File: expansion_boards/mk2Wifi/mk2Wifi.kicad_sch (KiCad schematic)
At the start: 21 parts, among them J2 USB_C_Receptacle_USB2.0, J4 OLED, SW1 SW_Push, U1 ESP32-C3-MINI-1, U2 AP2112K-3.3

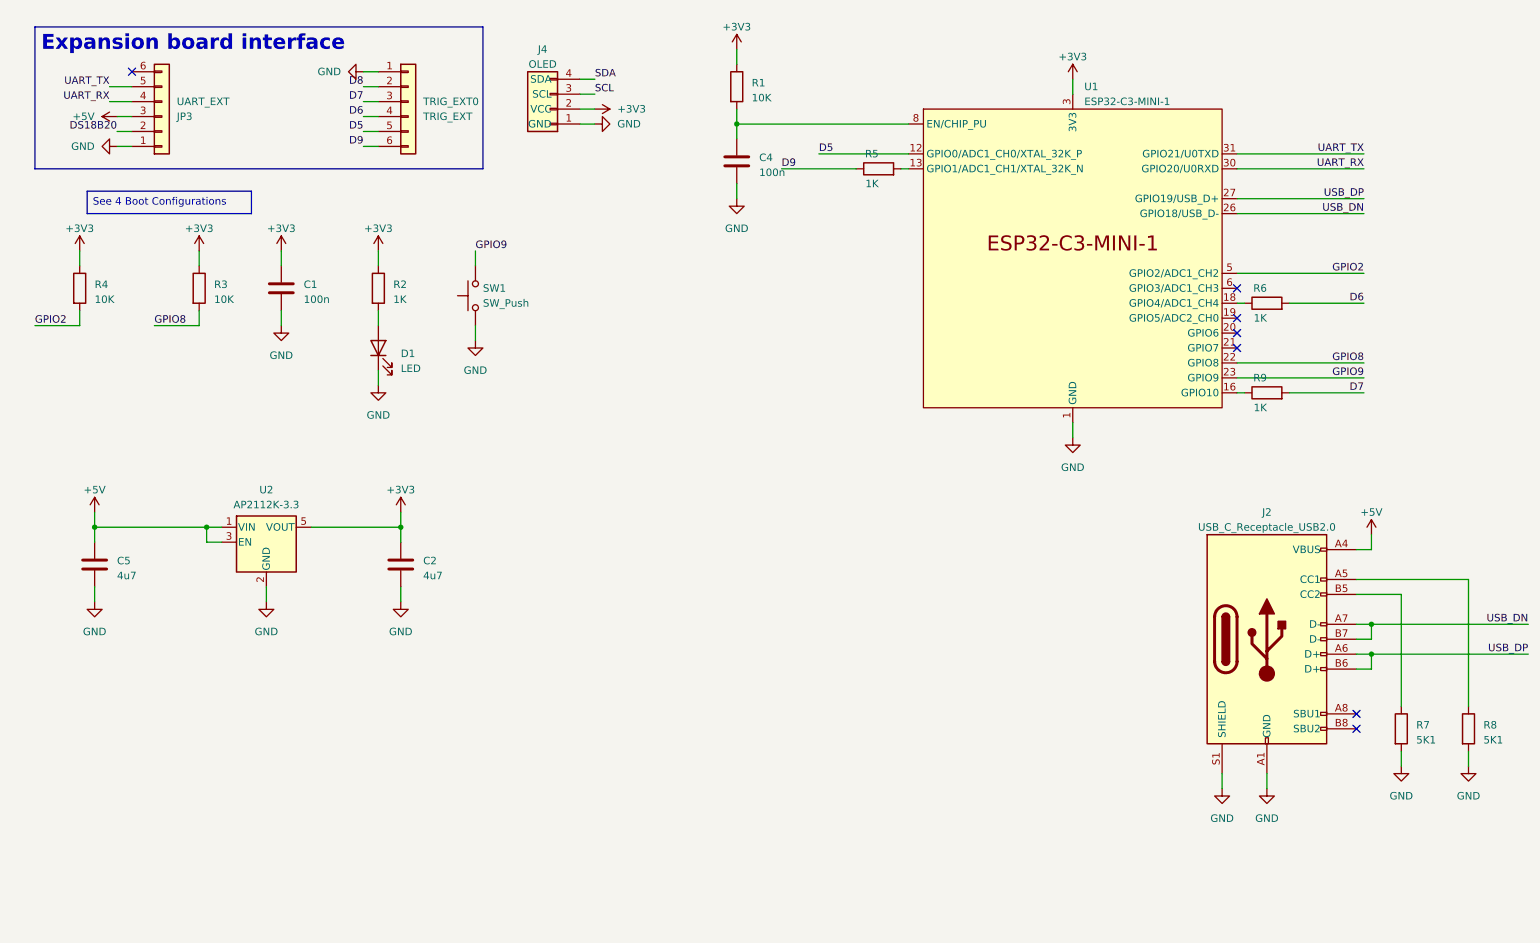
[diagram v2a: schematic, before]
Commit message: Wire remaining ESP32-C3 GPIOs and fix mk2Wifi ERC errors
Connect GPIO3 (DS18B20), GPIO5 (SDA), GPIO6 (SCL) directly and
GPIO7 (D8) through R11 (1K) protection resistor. Fix duplicate
power symbol references (#PWR01/03/04/08), add UserDef symbol
library to sym-lib-table, and add PWR_FLAG symbols to +5V, +3.3V,
and GND nets to resolve all ERC errors.

Co-Authored-By: Claude Opus 4.6 <noreply@anthropic.com>
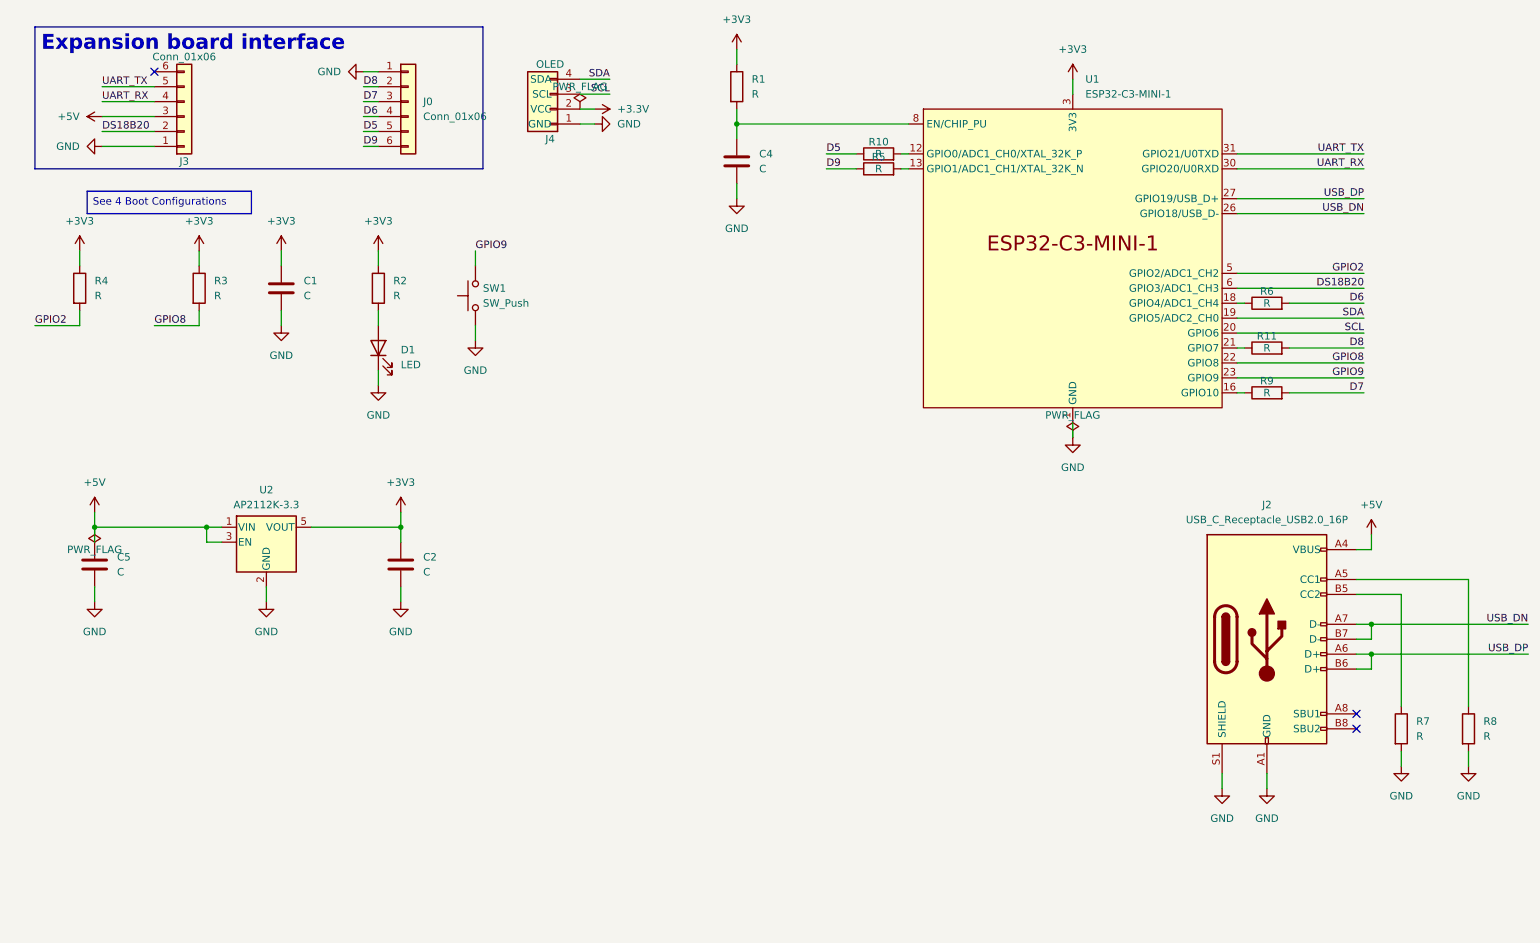
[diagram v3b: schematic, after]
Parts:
- added R10, R11: R, symbol Device:R
- C1, C4: value 100n -> C; footprint Capacitor_SMD:C_0402_1005Metric -> (none); LCSC PN C1525 -> (none)
- C2, C5: value 4u7 -> C; footprint Capacitor_SMD:C_0603_1608Metric -> (none); LCSC PN C19666 -> (none)
- D1: footprint LED_SMD:LED_0603_1608Metric -> (none); LCSC PN C2286 -> (none)
- J0: renamed from TRIG_EXT0; value TRIG_EXT -> Conn_01x06; footprint Connector_PinSocket_2.54mm:PinSocket_1x06_P2.54mm_Vertical -> (none)
- J2: value USB_C_Receptacle_USB2.0 -> USB_C_Receptacle_USB2.0_16P; footprint valcon-usb:CSP-USC16-TR -> (none); symbol Connector:USB_C_Receptacle_USB2.0 -> Connector:USB_C_Receptacle_USB2.0_16P; LCSC PN C2765186 -> (none)
- J3: renamed from JP3; value UART_EXT -> Conn_01x06; footprint Connector_PinSocket_2.54mm:PinSocket_1x06_P2.54mm_Vertical -> (none)
- J4: footprint Connector_Molex:Molex_SL_171971-0004_1x04_P2.54mm_Vertical -> (none); Option X -> (none)
- R1, R3, R4: value 10K -> R; footprint Resistor_SMD:R_0402_1005Metric -> (none); LCSC PN C25744 -> (none)
- R2: value 1K -> R; footprint Resistor_SMD:R_0402_1005Metric -> (none); LCSC PN C11702 -> (none)
- R5, R6, R9: value 1K -> R; footprint Resistor_SMD:R_0402_1005Metric -> (none)
- R7, R8: value 5K1 -> R; footprint Resistor_SMD:R_0402_1005Metric -> (none); LCSC PN C25905 -> (none)
- SW1: footprint Button_Switch_SMD:SW_Tactile_SPST_NO_Straight_CK_PTS636Sx25SMTRLFS -> (none); LCSC PN C2689642 -> (none)
- U1: LCSC PN C2838502 -> (none)
- U2: LCSC PN C23380830 -> (none)
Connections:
- net +3V3: no longer J4.2 (VCC)
- net D5: now also R10.1; no longer U1.12 (GPIO0/ADC1_CH0/XTAL_32K_P)
- net D8: now also R11.2
- net DS18B20: now also U1.6 (GPIO3/ADC1_CH3)
- net SCL: now also U1.20 (GPIO6)
- net SDA: now also U1.19 (GPIO5/ADC2_CH0)
- net at U1.21 (GPIO7): now also R11.1
- new net: R10.2, U1.12 (GPIO0/ADC1_CH0/XTAL_32K_P)
- new net +3.3V: J4.2 (VCC)
- no-connect marks 7 -> 3
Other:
- moved on the sheet: J3

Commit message: Assign footprints and values to all mk2Wifi components
Set resistor values (1K, 5K1, 10K) and 0402 footprints for R1-R11,
capacitor values (100n, 4u7) with 0402/0603 footprints for C1-C5,
and footprints for D1 (LED 0603), SW1 (CK PTS636S tactile), J0 and
J3 (PinSocket 1x06). Values and footprints match emonWiFi reference
design by circuit function.

Co-Authored-By: Claude Opus 4.6 <noreply@anthropic.com>
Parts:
- C1, C4: value C -> 100n; footprint (none) -> Capacitor_SMD:C_0402_1005Metric
- C2, C5: value C -> 4u7; footprint (none) -> Capacitor_SMD:C_0603_1608Metric
- D1: footprint (none) -> LED_SMD:LED_0603_1608Metric
- J0, J3: footprint (none) -> Connector_PinSocket_2.54mm:PinSocket_1x06_P2.54mm_Vertical
- J2: footprint (none) -> valcon-usb:CSP-USC16-TR
- J4: footprint (none) -> Connector_Molex:Molex_SL_171971-0004_1x04_P2.54mm_Vertical
- R1, R3, R4: value R -> 10K; footprint (none) -> Resistor_SMD:R_0402_1005Metric
- R10, R11, R2, R5, R6, R9: value R -> 1K; footprint (none) -> Resistor_SMD:R_0402_1005Metric
- R7, R8: value R -> 5K1; footprint (none) -> Resistor_SMD:R_0402_1005Metric
- SW1: footprint (none) -> Button_Switch_SMD:SW_Tactile_SPST_NO_Straight_CK_PTS636Sx25SMTRLFS

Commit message: Finalize mk2Wifi PCB layout, project settings, and 3D model
Update PCB layout with component placement and routing for all
newly footprinted parts. Adjust zone clearance (0.25mm) and via
sizes (0.8/0.4mm) in project settings. Add UserDef footprint
library to fp-lib-table. Include ESP32-C3-MINI-1 STEP 3D model.

Co-Authored-By: Claude Opus 4.6 <noreply@anthropic.com>
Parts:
- J0: value Conn_01x06 -> TRIG_EXT
- J3: value Conn_01x06 -> UART_EXT
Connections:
- net at R9.1: now also U1.13 (GPIO1/ADC1_CH1/XTAL_32K_N); no longer U1.16 (GPIO10)
- net at R10.2: now also U1.18 (GPIO4/ADC1_CH4); no longer U1.12 (GPIO0/ADC1_CH0/XTAL_32K_P)
- net at R5.2: now also U1.21 (GPIO7); no longer U1.13 (GPIO1/ADC1_CH1/XTAL_32K_N)
- net at R6.1: now also U1.16 (GPIO10); no longer U1.18 (GPIO4/ADC1_CH4)
- net at R11.1: now also U1.12 (GPIO0/ADC1_CH0/XTAL_32K_P); no longer U1.21 (GPIO7)
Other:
- moved on the sheet: R10, R11, R5, R6, R9
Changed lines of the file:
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@@
 	(wire
 		(pts
-			(xy 163.83 39.37) (xy 165.1 39.37)
+			(xy 220.98 59.69) (xy 242.57 59.69)
 		)
 		(stroke
@@
 	(wire
 		(pts
-			(xy 220.98 59.69) (xy 242.57 59.69)
+			(xy 156.21 41.91) (xy 151.13 41.91)
 		)
 		(stroke
@@
 	(wire
 		(pts
-			(xy 229.87 80.01) (xy 242.57 80.01)
+			(xy 220.98 80.01) (xy 222.25 80.01)
 		)
 		(stroke
@@
 	(wire
 		(pts
-			(xy 151.13 39.37) (xy 156.21 39.37)
+			(xy 242.57 64.77) (xy 229.87 64.77)
 		)
 		(stroke
@@
 	(wire
 		(pts
+			(xy 220.98 64.77) (xy 222.25 64.77)
+		)
+		(stroke
+			(width 0)
+			(type default)
+		)
+	)
+	(wire
+		(pts
 			(xy 109.22 31.75) (xy 111.76 31.75)
 		)
@@
 	(wire
 		(pts
-			(xy 151.13 41.91) (xy 156.21 41.91)
+			(xy 242.57 72.39) (xy 229.87 72.39)
 		)
 		(stroke
@@
 	(wire
 		(pts
-			(xy 241.3 121.92) (xy 243.84 121.92)
+			(xy 220.98 72.39) (xy 222.25 72.39)
 		)
 		(stroke
@@
 	(wire
 		(pts
-			(xy 163.83 41.91) (xy 165.1 41.91)
+			(xy 241.3 121.92) (xy 243.84 121.92)
 		)
 		(stroke
@@
 	(wire
 		(pts
-			(xy 241.3 111.76) (xy 260.35 111.76)
+			(xy 163.83 41.91) (xy 165.1 41.91)
 		)
 		(stroke
@@
 	(wire
 		(pts
-			(xy 135.89 34.29) (xy 165.1 34.29)
+			(xy 241.3 111.76) (xy 260.35 111.76)
 		)
 		(stroke
@@
 	(wire
 		(pts
-			(xy 26.67 113.03) (xy 26.67 115.57)
+			(xy 135.89 34.29) (xy 165.1 34.29)
 		)
 		(stroke
@@
 	(wire
 		(pts
-			(xy 260.35 111.76) (xy 260.35 133.35)
+			(xy 26.67 113.03) (xy 26.67 115.57)
 		)
 		(stroke
@@
 	(wire
 		(pts
-			(xy 135.89 44.45) (xy 135.89 46.99)
+			(xy 260.35 111.76) (xy 260.35 133.35)
 		)
 		(stroke
@@
 	(wire
 		(pts
-			(xy 58.42 66.04) (xy 58.42 68.58)
+			(xy 135.89 44.45) (xy 135.89 46.99)
 		)
 		(stroke
@@
 	(wire
 		(pts
-			(xy 220.98 80.01) (xy 222.25 80.01)
+			(xy 58.42 66.04) (xy 58.42 68.58)
 		)
 		(stroke
@@
 	(wire
 		(pts
-			(xy 220.98 64.77) (xy 222.25 64.77)
-		)
-		(stroke
-			(width 0)
-			(type default)
-		)
-	)
-	(wire
-		(pts
 			(xy 220.98 69.85) (xy 242.57 69.85)
 		)
@@
 	(wire
 		(pts
-			(xy 220.98 77.47) (xy 242.57 77.47)
+			(xy 163.83 39.37) (xy 165.1 39.37)
 		)
 		(stroke
@@
 	(wire
 		(pts
-			(xy 220.98 72.39) (xy 222.25 72.39)
+			(xy 220.98 77.47) (xy 242.57 77.47)
 		)
 		(stroke
@@
 	(wire
 		(pts
-			(xy 229.87 64.77) (xy 242.57 64.77)
+			(xy 229.87 80.01) (xy 242.57 80.01)
 		)
 		(stroke
@@
 	(wire
 		(pts
-			(xy 229.87 72.39) (xy 242.57 72.39)
+			(xy 156.21 39.37) (xy 151.13 39.37)
 		)
 		(stroke
@@
 	)
 	(label "D5"
-		(at 151.13 39.37 0)
+		(at 242.57 64.77 180)
 		(effects
 			(font
 				(size 1.27 1.27)
 			)
-			(justify left bottom)
+			(justify right bottom)
 		)
 	)
@@
 	)
 	(label "D9"
-		(at 151.13 41.91 0)
+		(at 242.57 72.39 180)
 		(effects
 			(font
 				(size 1.27 1.27)
 			)
-			(justify left bottom)
+			(justify right bottom)
 		)
 	)
@@
 	)
 	(label "D6"
-		(at 242.57 64.77 180)
+		(at 242.57 80.01 180)
 		(effects
 			(font
@@
 	)
 	(label "D8"
-		(at 242.57 72.39 180)
+		(at 151.13 39.37 0)
 		(effects
 			(font
 				(size 1.27 1.27)
 			)
-			(justify right bottom)
+			(justify left bottom)
 		)
 	)
@@
 	)
 	(label "D7"
-		(at 242.57 80.01 180)
+		(at 151.13 41.91 0)
 		(effects
 			(font
 				(size 1.27 1.27)
 			)
-			(justify right bottom)
+			(justify left bottom)
 		)
 	)
@@
 	(symbol
 		(lib_id "Device:R")
-		(at 226.06 80.01 90)
+		(at 160.02 41.91 270)
 		(unit 1)
 		(exclude_from_sim no)
@@
 		(dnp no)
 		(property "Reference" "R9"
-			(at 226.06 77.978 90)
+			(at 160.02 43.942 90)
 			(effects
 				(font
@@
 		)
 		(property "Value" "1K"
-			(at 226.06 80.01 90)
+			(at 160.02 41.91 90)
 			(effects
 				(font
@@
 		)
 		(property "Footprint" "Resistor_SMD:R_0402_1005Metric"
-			(at 226.06 81.788 90)
+			(at 160.02 40.132 90)
 			(effects
 				(font
@@
 		)
 		(property "Datasheet" "~"
-			(at 226.06 80.01 0)
+			(at 160.02 41.91 0)
 			(effects
 				(font
@@
 		)
 		(property "Description" "Resistor"
-			(at 226.06 80.01 0)
+			(at 160.02 41.91 0)
 			(effects
 				(font
@@
 	(symbol
 		(lib_id "Device:R")
-		(at 160.02 39.37 90)
+		(at 226.06 64.77 270)
 		(unit 1)
 		(exclude_from_sim no)
@@
 		(dnp no)
 		(property "Reference" "R10"
-			(at 160.02 37.338 90)
+			(at 226.314 67.31 90)
 			(effects
 				(font
@@
 		)
 		(property "Value" "1K"
-			(at 160.02 39.37 90)
+			(at 226.314 64.77 90)
 			(effects
 				(font
@@
 		)
 		(property "Footprint" "Resistor_SMD:R_0402_1005Metric"
-			(at 160.02 41.148 90)
+			(at 226.06 62.992 90)
 			(effects
 				(font
@@
 		)
 		(property "Datasheet" "~"
-			(at 160.02 39.37 0)
+			(at 226.06 64.77 0)
 			(effects
 				(font
@@
 		)
 		(property "Description" "Resistor"
-			(at 160.02 39.37 0)
+			(at 226.06 64.77 0)
 			(effects
 				(font
@@
 			)
 		)
-		(property "Value" "Conn_01x06"
+		(property "Value" "TRIG_EXT"
 			(at 82.55 33.0199 0)
 			(effects
@@
 			)
 		)
-		(property "Value" "Conn_01x06"
+		(property "Value" "UART_EXT"
 			(at 41.91 22.86 0)
 			(effects
@@
 	(symbol
 		(lib_id "Device:R")
-		(at 226.06 72.39 90)
+		(at 160.02 39.37 270)
 		(unit 1)
 		(exclude_from_sim no)
@@
 		(dnp no)
 		(property "Reference" "R11"
-			(at 226.06 70.358 90)
+			(at 160.02 37.338 90)
 			(effects
 				(font
@@
 		)
 		(property "Value" "1K"
-			(at 226.06 72.39 90)
+			(at 160.02 39.37 90)
 			(effects
 				(font
@@
 		)
 		(property "Footprint" "Resistor_SMD:R_0402_1005Metric"
-			(at 226.06 74.168 90)
+			(at 160.02 37.592 90)
 			(effects
 				(font
@@
 		)
 		(property "Datasheet" "~"
-			(at 226.06 72.39 0)
+			(at 160.02 39.37 0)
 			(effects
 				(font
@@
 		)
 		(property "Description" "Resistor"
-			(at 226.06 72.39 0)
+			(at 160.02 39.37 0)
 			(effects
 				(font
@@
 	(symbol
 		(lib_id "Device:R")
-		(at 160.02 41.91 90)
+		(at 226.06 72.39 270)
 		(unit 1)
 		(exclude_from_sim no)
@@
 		(dnp no)
 		(property "Reference" "R5"
-			(at 160.02 39.878 90)
+			(at 226.314 69.85 90)
 			(effects
 				(font
@@
 		)
 		(property "Value" "1K"
-			(at 160.02 41.91 90)
+			(at 226.314 72.39 90)
 			(effects
 				(font
@@
 		)
 		(property "Footprint" "Resistor_SMD:R_0402_1005Metric"
-			(at 160.02 43.688 90)
+			(at 226.06 70.612 90)
 			(effects
 				(font
@@
 		)
 		(property "Datasheet" "~"
-			(at 160.02 41.91 0)
+			(at 226.06 72.39 0)
 			(effects
 				(font
@@
 		)
 		(property "Description" "Resistor"
-			(at 160.02 41.91 0)
+			(at 226.06 72.39 0)
 			(effects
 				(font
@@
 	(symbol
 		(lib_id "Device:R")
-		(at 226.06 64.77 90)
+		(at 226.06 80.01 90)
 		(unit 1)
 		(exclude_from_sim no)
@@
 		(dnp no)
 		(property "Reference" "R6"
-			(at 226.06 62.738 90)
+			(at 226.06 77.978 90)
 			(effects
 				(font
@@
 		)
 		(property "Value" "1K"
-			(at 226.06 64.77 90)
+			(at 226.06 80.01 90)
 			(effects
 				(font
@@
 		)
 		(property "Footprint" "Resistor_SMD:R_0402_1005Metric"
-			(at 226.06 66.548 90)
+			(at 226.06 81.788 90)
 			(effects
 				(font
@@
 		)
 		(property "Datasheet" "~"
-			(at 226.06 64.77 0)
+			(at 226.06 80.01 0)
 			(effects
 				(font
@@
 		)
 		(property "Description" "Resistor"
-			(at 226.06 64.77 0)
+			(at 226.06 80.01 0)
 			(effects
 				(font
